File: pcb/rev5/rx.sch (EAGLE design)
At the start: 34 parts, among them IC1 STM32F042F4, IC2 NRF24L01ALT1, SW1 SW_3POS_DEVSW_3POS_OFFICIAL, SW2 324_SW324_SWITCH_FOOT_HOLE, U1 USBC_16P, U2 XC6206_DEV, Y1 16MHz_12pF

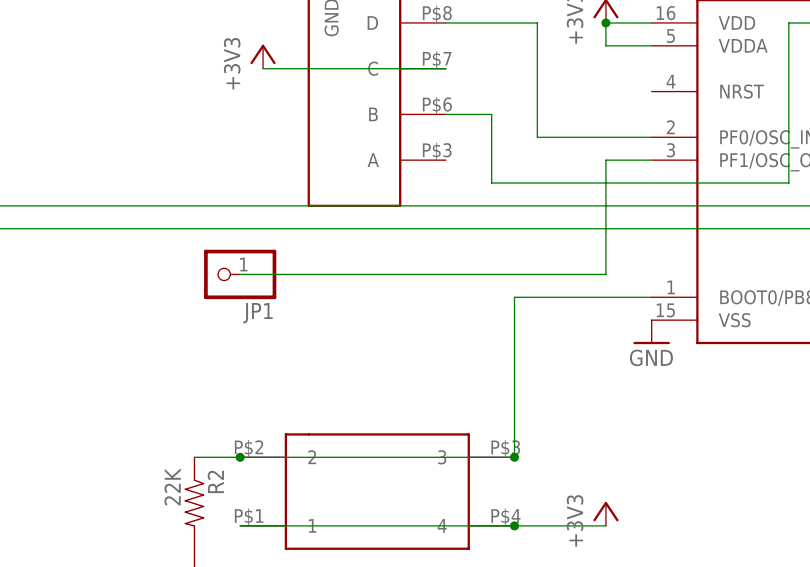
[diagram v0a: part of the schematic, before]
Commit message: added trig_out on RX, preparing for next production run
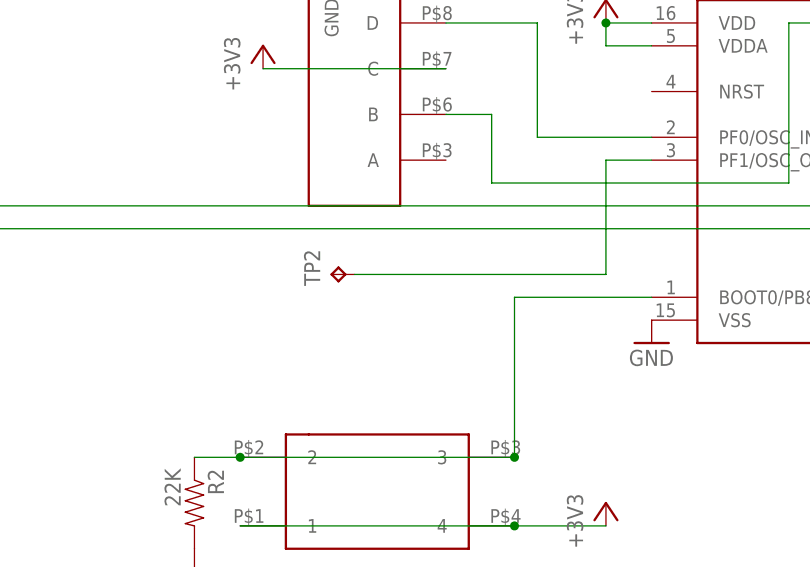
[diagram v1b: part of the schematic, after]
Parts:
- removed JP1: (no value), adafruit_changed:PINHD-1X1CB
- added TP2: TPTP12R, testpad:TPTP12R
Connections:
- net N$19: now also TP2.TP; no longer JP1.1
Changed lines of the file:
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@@
 <part name="R6" library="joyAnalog" deviceset="RESISTOR" device="0805-RES" value="1 Ohm"/>
 <part name="C14" library="clock" deviceset="CAP" device="0805" value="4.7uF"/>
+<part name="TP2" library="testpad" library_urn="urn:adsk.eagle:library:385" deviceset="TP" device="TP12R" package3d_urn="urn:adsk.eagle:package:27963/1"/>
 <part name="U1" library="my_usbc_16p" deviceset="USBC_16P" device=""/>
 <part name="SW1" library="3pos_slide_switch_centered" deviceset="SW_3POS_DEV" device="SW_3POS_OFFICIAL"/>
-<part name="JP1" library="adafruit_changed" deviceset="PINHD-1X1" device="CB"/>
 </parts>
 <sheets>
@@
 <instance part="R6" gate="G$1" x="116.84" y="55.88" rot="R270"/>
 <instance part="C14" gate="G$1" x="147.32" y="43.18"/>
+<instance part="TP2" gate="G$1" x="-22.86" y="-2.54" rot="R90"/>
 <instance part="U1" gate="G$1" x="-172.72" y="-22.86" rot="MR0"/>
 <instance part="SW1" gate="G$1" x="-22.86" y="17.78" rot="R270"/>
-<instance part="JP1" gate="G$1" x="-35.56" y="-2.54" rot="R180"/>
 </instances>
 <busses>
@@
 <wire x1="12.7" y1="10.16" x2="7.62" y2="10.16" width="0.1524" layer="91"/>
 <wire x1="7.62" y1="10.16" x2="7.62" y2="-2.54" width="0.1524" layer="91"/>
-<wire x1="7.62" y1="-2.54" x2="-33.02" y2="-2.54" width="0.1524" layer="91"/>
-<pinref part="JP1" gate="G$1" pin="1"/>
+<wire x1="7.62" y1="-2.54" x2="-20.32" y2="-2.54" width="0.1524" layer="91"/>
+<pinref part="TP2" gate="G$1" pin="TP"/>
 </segment>
 </net>
@@
 will not be understood (or retained) with this version.
 </note>
+<note version="8.3" severity="warning">
+Since Version 8.3, EAGLE supports the association of 3D packages
+with devices in libraries, schematics, and board files. Those 3D
+packages will not be understood (or retained) with this version.
+</note>
 </compatibility>
